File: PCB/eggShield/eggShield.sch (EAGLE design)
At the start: 22 parts

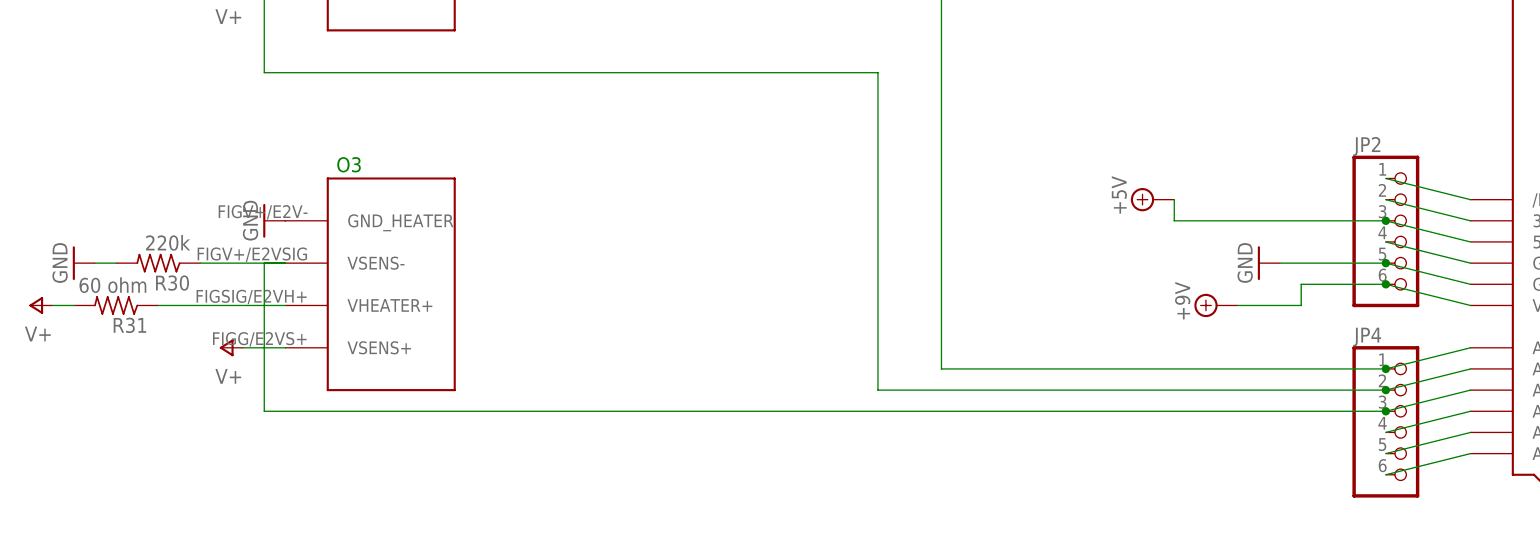
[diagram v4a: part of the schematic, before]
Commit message: sensor update, needs i2c bus
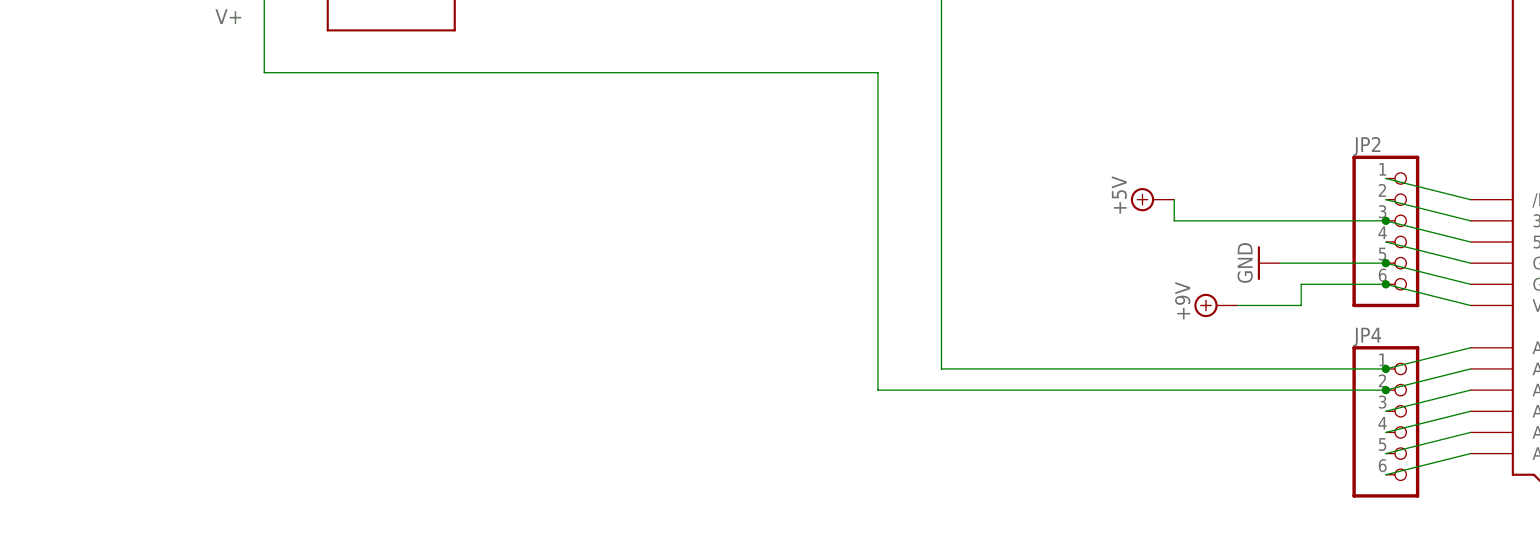
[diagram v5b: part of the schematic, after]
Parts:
- removed R30: 220k, rcl:R-US_R1206
- removed R31: 60 ohm, rcl:R-US_R1206
- removed U$9: E2V Ozone, ricardo:E2V
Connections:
- removed net N$45: R31.1, U$9.VHEATER+
- net 1.8: no longer R30.2, U$9.GND_HEATER
- net N$55: no longer R30.1, U$9.VSENS-
- net V+: no longer R31.2, U$9.VSENS+
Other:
- note removed: "O3"
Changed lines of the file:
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@@
 <part name="R7" library="rcl" deviceset="R-US_" device="R1206" value="34 ohm"/>
 <part name="P+6" library="supply1" deviceset="V+" device=""/>
-<part name="U$9" library="ricardo" deviceset="E2V" device="" value="E2V Ozone"/>
-<part name="GND28" library="supply1" deviceset="GND" device=""/>
-<part name="P+11" library="supply1" deviceset="V+" device=""/>
-<part name="R30" library="rcl" deviceset="R-US_" device="R1206" value="220k"/>
-<part name="GND33" library="supply1" deviceset="GND" device=""/>
-<part name="R31" library="rcl" deviceset="R-US_" device="R1206" value="60 ohm"/>
-<part name="P+12" library="supply1" deviceset="V+" device=""/>
 <part name="SUPPLY16" library="supply2" deviceset="+9V" device=""/>
 <part name="GND81" library="supply1" deviceset="GND" device=""/>
@@
 <text x="419.1" y="213.36" size="1.778" layer="91">+9V TEST PADS</text>
 <text x="33.02" y="252.73" size="1.778" layer="91">NO2</text>
-<text x="34.036" y="168.402" size="1.778" layer="91">O3</text>
 <text x="33.02" y="212.09" size="1.778" layer="91">CO</text>
 <text x="398.78" y="182.88" size="3.81" layer="97">Possibly Useful stuff</text>
@@
 <instance part="R7" gate="G$1" x="7.62" y="236.22" rot="R180"/>
 <instance part="P+6" gate="1" x="20.32" y="231.14" rot="R90"/>
-<instance part="U$9" gate="G$1" x="48.26" y="157.48"/>
-<instance part="GND28" gate="1" x="25.4" y="162.56" rot="R270"/>
-<instance part="P+11" gate="1" x="-2.54" y="152.4" rot="R90"/>
-<instance part="R30" gate="G$1" x="12.7" y="157.48" rot="R180"/>
-<instance part="GND33" gate="1" x="2.54" y="157.48" rot="R270"/>
-<instance part="R31" gate="G$1" x="7.62" y="152.4" rot="R180"/>
-<instance part="P+12" gate="1" x="20.32" y="147.32" rot="R90"/>
 <instance part="SUPPLY16" gate="G$1" x="431.8" y="241.3"/>
 <instance part="GND81" gate="1" x="431.8" y="220.98"/>
@@
 </segment>
 <segment>
-<pinref part="U$9" gate="G$1" pin="GND_HEATER"/>
-<pinref part="GND28" gate="1" pin="GND"/>
-</segment>
-<segment>
-<pinref part="R30" gate="G$1" pin="2"/>
-<pinref part="GND33" gate="1" pin="GND"/>
-<wire x1="5.08" y1="157.48" x2="7.62" y2="157.48" width="0.1524" layer="91"/>
-</segment>
-<segment>
 <pinref part="GND81" gate="1" pin="GND"/>
 <wire x1="431.8" y1="223.52" x2="431.8" y2="228.6" width="0.1524" layer="91"/>
@@
 <pinref part="P+6" gate="1" pin="V+"/>
 <wire x1="22.86" y1="231.14" x2="27.94" y2="231.14" width="0.1524" layer="91"/>
-</segment>
-<segment>
-<pinref part="P+11" gate="1" pin="V+"/>
-<pinref part="R31" gate="G$1" pin="2"/>
-<wire x1="0" y1="152.4" x2="2.54" y2="152.4" width="0.1524" layer="91"/>
-</segment>
-<segment>
-<pinref part="U$9" gate="G$1" pin="VSENS+"/>
-<pinref part="P+12" gate="1" pin="V+"/>
-<wire x1="22.86" y1="147.32" x2="27.94" y2="147.32" width="0.1524" layer="91"/>
 </segment>
 <segment>
@@
 <pinref part="R7" gate="G$1" pin="1"/>
 <wire x1="27.94" y1="236.22" x2="12.7" y2="236.22" width="0.1524" layer="91"/>
-</segment>
-</net>
-<net name="N$45" class="0">
-<segment>
-<pinref part="U$9" gate="G$1" pin="VHEATER+"/>
-<pinref part="R31" gate="G$1" pin="1"/>
-<wire x1="27.94" y1="152.4" x2="12.7" y2="152.4" width="0.1524" layer="91"/>
 </segment>
 </net>
@@
 <net name="N$55" class="0">
 <segment>
-<pinref part="U$9" gate="G$1" pin="VSENS-"/>
-<pinref part="R30" gate="G$1" pin="1"/>
-<wire x1="17.78" y1="157.48" x2="27.94" y2="157.48" width="0.1524" layer="91"/>
-<wire x1="27.94" y1="157.48" x2="25.4" y2="157.48" width="0.1524" layer="91"/>
-<wire x1="25.4" y1="157.48" x2="25.4" y2="139.7" width="0.1524" layer="91"/>
 <pinref part="JP4" gate="A" pin="3"/>
 <pinref part="U$2" gate="G$1" pin="A2"/>
 <wire x1="160.02" y1="139.7" x2="170.18" y2="142.24" width="0.1524" layer="91"/>
-<wire x1="160.02" y1="139.7" x2="25.4" y2="139.7" width="0.1524" layer="91"/>
-<junction x="160.02" y="139.7"/>
-</segment>
-</net>
+</segment>
+</net>

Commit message: added pdfs
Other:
- note added: "power stuff"
- note removed: "+9V TEST PADS"
- note removed: "Possibly Useful stuff"
- note removed: "V+/5V TEST PADS"
- note removed: "power"
- moved on the sheet: +9V2, C6, C7, JP23, LD1085, LED4, R21, R22, R5, R7

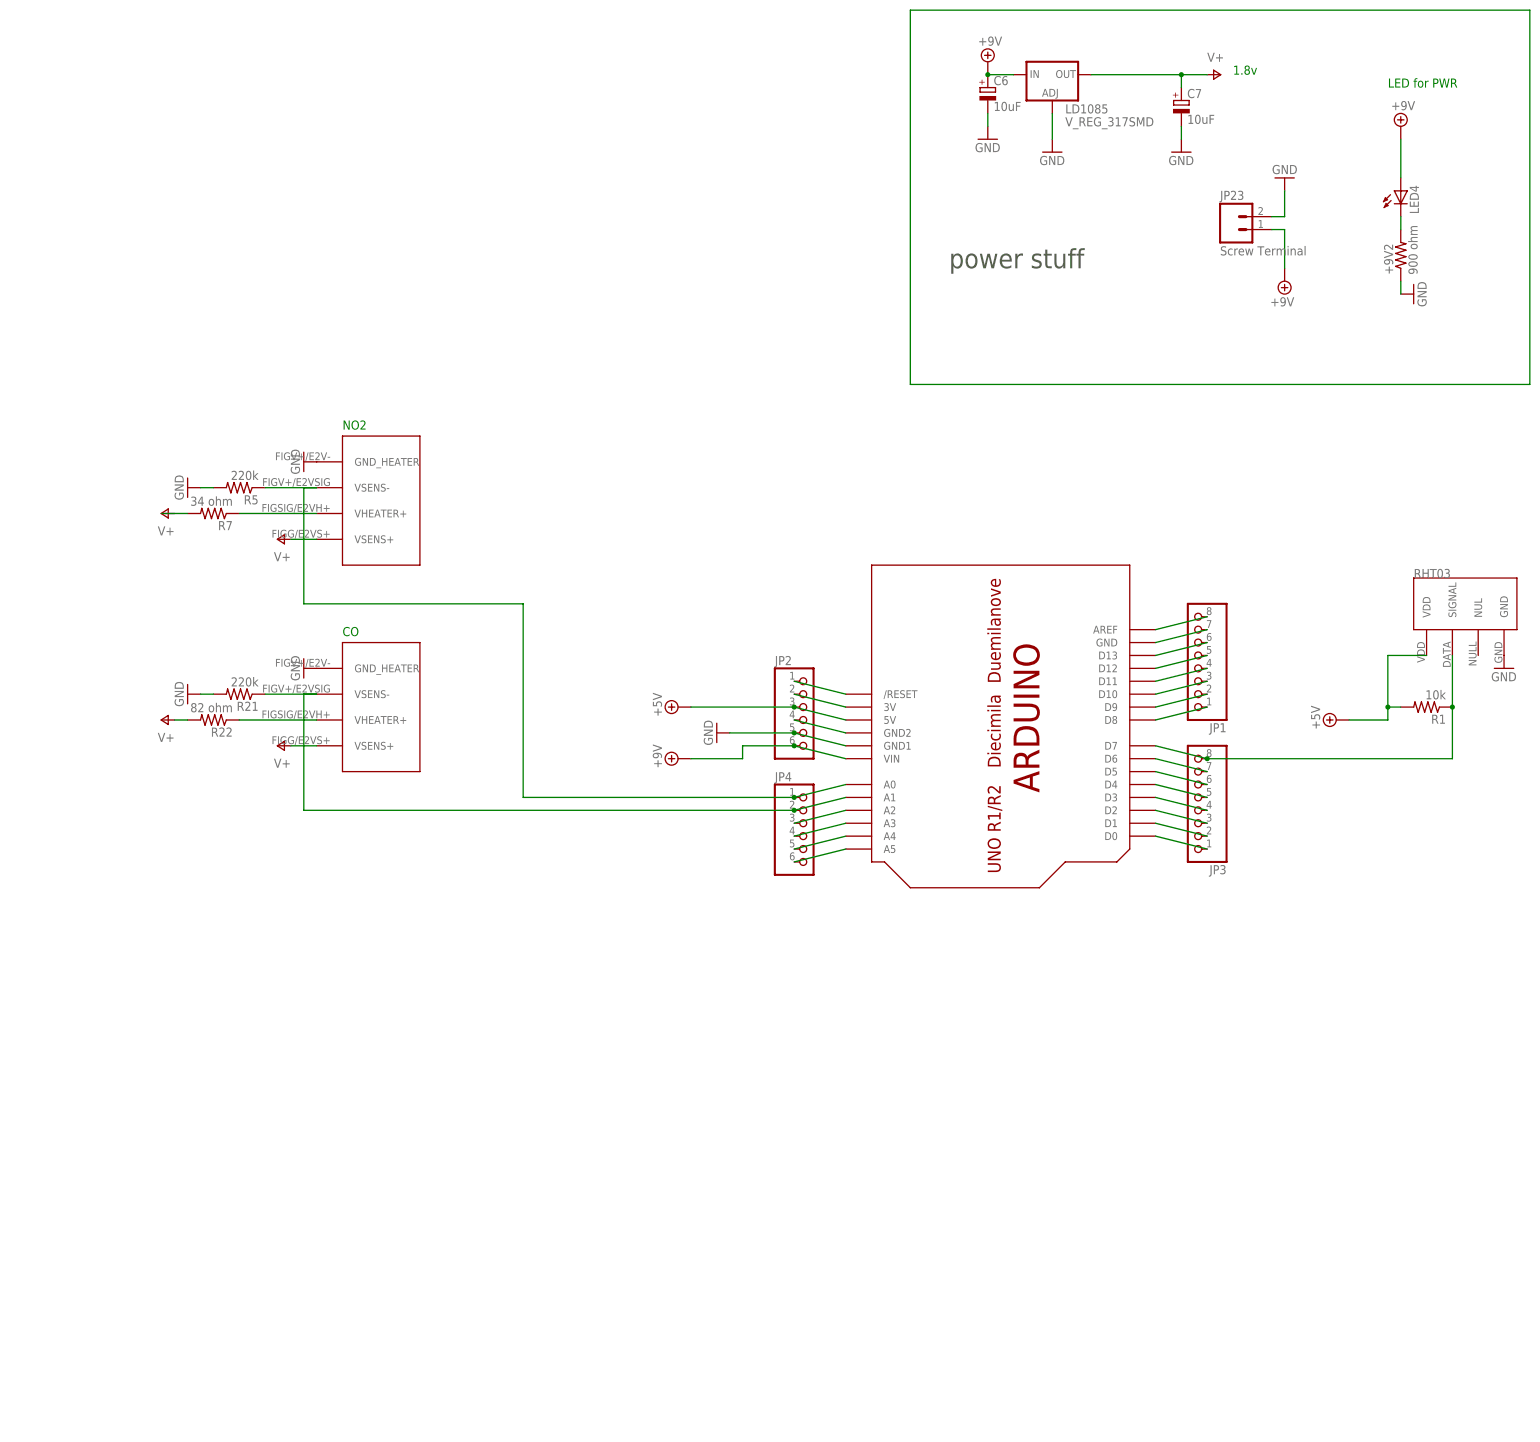
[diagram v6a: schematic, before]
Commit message: updates to the layout and schematics, bringing in elements of the CMOS breakout module
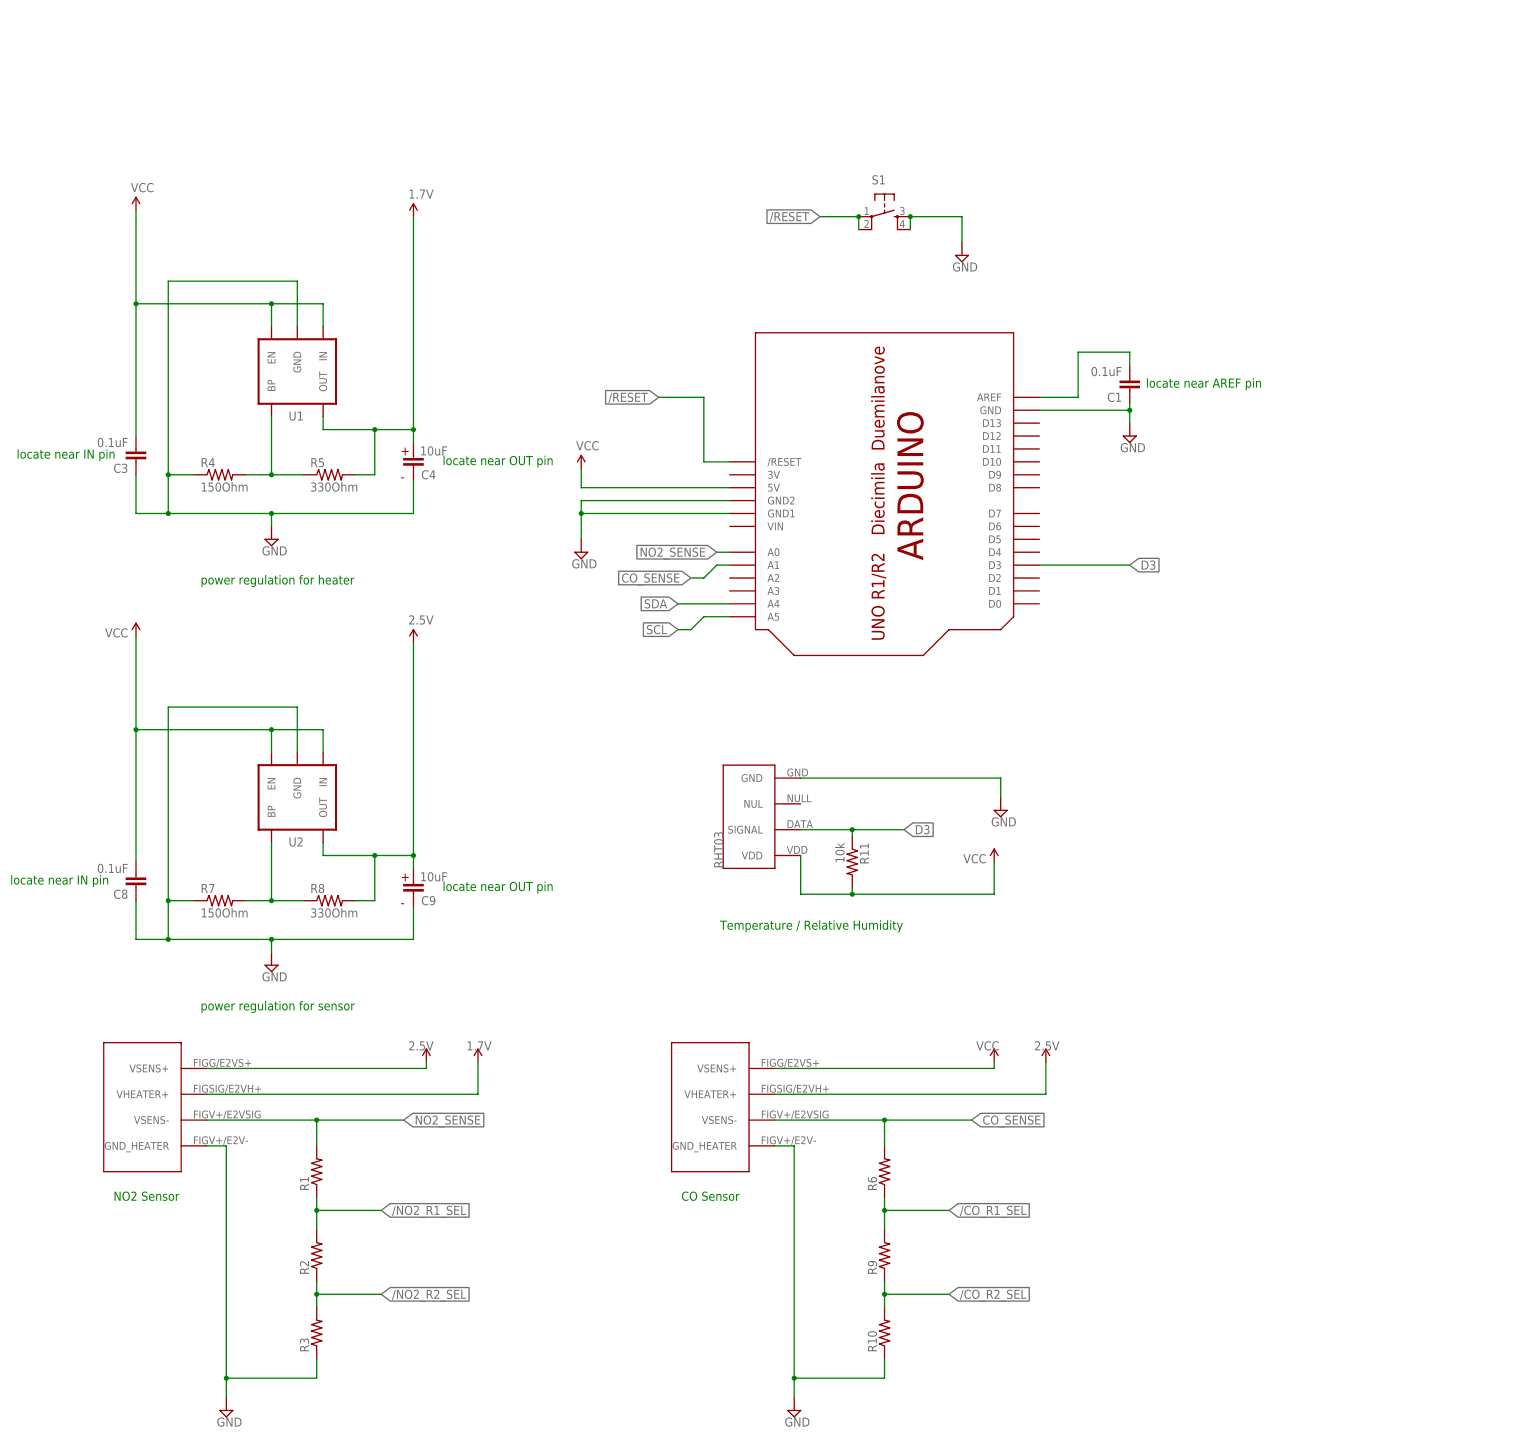
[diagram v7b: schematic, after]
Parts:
- removed +9V2: 900 ohm, rcl:R-US_R1206
- removed C6, C7: 10uF, resistor:CPOL-EUCT3216
- removed JP1, JP3: (no value), adafruit:PINHD-1X8BIG
- removed JP2, JP4: (no value), adafruit:PINHD-1X6B
- removed JP23: Screw Terminal, SparkFun:M025MM
- removed LD1085: V_REG_317SMD, SparkFun:V_REG_317SMD
- removed LED4: (no value), SparkFun:LED3MM
- removed NO2: E2V NO2, ricardo:E2V
- removed R21: 220k, rcl:R-US_R1206
- removed R22: 82 ohm, rcl:R-US_R1206
- removed U$13: E2V, ricardo:E2V
- removed U$14: RHT03, ricardo:RHT03
- added C1, C3, C8: 0.1uF, SparkFun:CAP0603-CAP
- added C4, C9: 10uF, wicked-device:EEE-1EA100WR
- added DHT22: RHT03, ricardo:RHT03
- added R10, R2, R3, R6, R9: (no value), SparkFun:RESISTOR0805-RES
- added R11: 10k, rcl:R-US_R1206
- added R4: 150Ohm, SparkFun:RESISTOR0805-RES
- added R8: 330Ohm, SparkFun:RESISTOR0805-RES
- added S1: (no value), SparkFun:TAC_SWITCHSMD
- added U$4: E2V, ricardo:E2V
- added U$7: ARDUINO-NOHOLE, adafruit:ARDUINO-NOHOLE
- added U1, U2: V_REG_LDOSMD, SparkFun:V_REG_LDOSMD
- R1: value 10k -> (none); device rcl:R-US_R1206 -> SparkFun:RESISTOR0805-RES
- R5: value 220k -> 330Ohm; device rcl:R-US_R1206 -> SparkFun:RESISTOR0805-RES
- R7: value 34 ohm -> 150Ohm; device rcl:R-US_R1206 -> SparkFun:RESISTOR0805-RES
- U$2: value ARDUINO-NODIM -> E2V; device adafruit:ARDUINO-NODIM -> ricardo:E2V
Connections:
- removed net +5V: JP2.3, R1.2, U$14.VDD, U$2.5V
- removed net +9V: C6.+, JP2.6, JP23.1, LD1085.IN, LED4.A, U$2.VIN
- removed net 1.8: +9V2.1, C6.-, C7.-, JP2.5, JP23.2, LD1085.ADJ, NO2.GND_HEATER, R21.2, R5.2, U$13.GND_HEATER, U$14.GND, U$2.GND1
- removed net A3: JP3.8, R1.1, U$14.SIGNAL, U$2.D7
- removed net N$10: JP4.4, U$2.A3
- removed net N$11: JP4.5, U$2.A4
- removed net N$12: JP4.6, U$2.A5
- removed net N$13: JP3.1, U$2.D0
- removed net N$14: JP3.2, U$2.D1
- removed net N$15: JP3.3, U$2.D2
- removed net N$16: JP3.4, U$2.D3
- removed net N$17: JP3.5, U$2.D4
- removed net N$18: JP3.6, U$2.D5
- removed net N$22: JP1.1, U$2.D8
- removed net N$23: JP1.2, U$2.D9
- removed net N$24: +9V2.2, LED4.C
- removed net N$25: JP1.3, U$2.D10
- removed net N$26: JP1.4, U$2.D11
- removed net N$27: JP1.5, U$2.D12
- removed net N$28: JP1.6, U$2.D13
- removed net N$29: JP1.7, U$2.GND
- removed net N$30: JP1.8, U$2.AREF
- removed net N$38: R22.1, U$13.VHEATER+
- removed net N$43: NO2.VHEATER+, R7.1
- removed net N$47: JP4.2, R21.1, U$13.VSENS-, U$2.A1
- removed net N$5: JP3.7, U$2.D6
- removed net N$50: JP4.1, NO2.VSENS-, R5.1, U$2.A0
- removed net N$55: JP4.3, U$2.A2
- removed net V+: C7.+, LD1085.OUT, NO2.VSENS+, R22.2, R7.2, U$13.VSENS+
- new net /CO_R1_SEL: R6.1, R9.2
- new net /CO_R2_SEL: R10.2, R9.1
- new net /NO2_R1_SEL: R1.1, R2.2
- new net /NO2_R2_SEL: R2.1, R3.2
- new net /RESET: S1.1, S1.2, U$7./RESET
- new net 1.7V: C4.1, R5.2, U$4.VHEATER+, U1.OUT
- new net 2.5V: C9.1, R8.2, U$2.VHEATER+, U$4.VSENS+, U2.OUT
- new net CO_SENSE: R6.2, U$2.VSENS-, U$7.A1
- new net D3: DHT22.SIGNAL, R11.1, U$7.D3
- new net GND: C1.1, C3.1, C4.2, C8.1, C9.2, DHT22.GND, R10.1, R3.1, R4.1, R7.1, S1.3, S1.4, U$2.GND_HEATER, U$4.GND_HEATER, U$7.GND, U$7.GND1, U$7.GND2, U1.GND, U2.GND
- new net NO2_SENSE: R1.2, U$4.VSENS-, U$7.A0
- new net SCL: U$7.A5
- new net SDA: U$7.A4
- new net VCC: C3.2, C8.2, DHT22.VDD, R11.2, U$2.VSENS+, U$7.5V, U1.EN, U1.IN, U2.EN, U2.IN
- net N$1: now also R4.2, R5.1, U1.BP; no longer JP2.1, U$2./RESET
- net N$2: now also R7.2, R8.1, U2.BP; no longer JP2.2, U$2.3V
- net N$4: now also C1.2, U$7.AREF; no longer JP2.4, U$2.GND2
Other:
- note added: "10uF"
- note added: "CO Sensor"
- note added: "NO2 Sensor"
- note added: "Temperature / Relative Humidity"
- note added: "locate near AREF pin"
- note added: "locate near IN pin"
- note added: "locate near OUT pin"
- note added: "power regulation for heater"
- note added: "power regulation for sensor"
- note removed: "1.8v"
- note removed: "CO"
- note removed: "LED for PWR"
- note removed: "NO2"
- note removed: "power stuff"
- moved on the sheet: R1, R5, R7
